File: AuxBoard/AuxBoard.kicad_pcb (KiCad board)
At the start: 2 copper layers, 2 parts, among them J1 ATX-24, J2 RPI4B

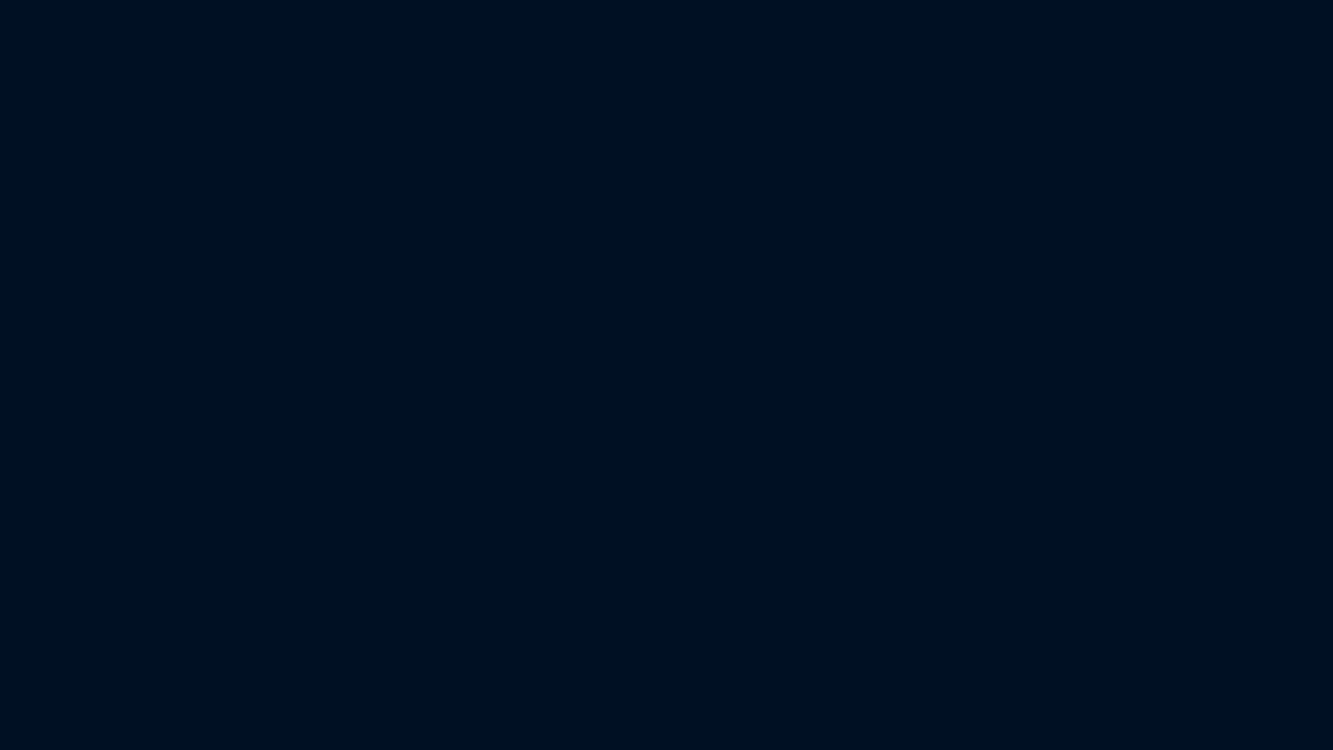
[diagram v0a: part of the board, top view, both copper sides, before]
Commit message: Added headers to handle comms with Matrices and Big LED
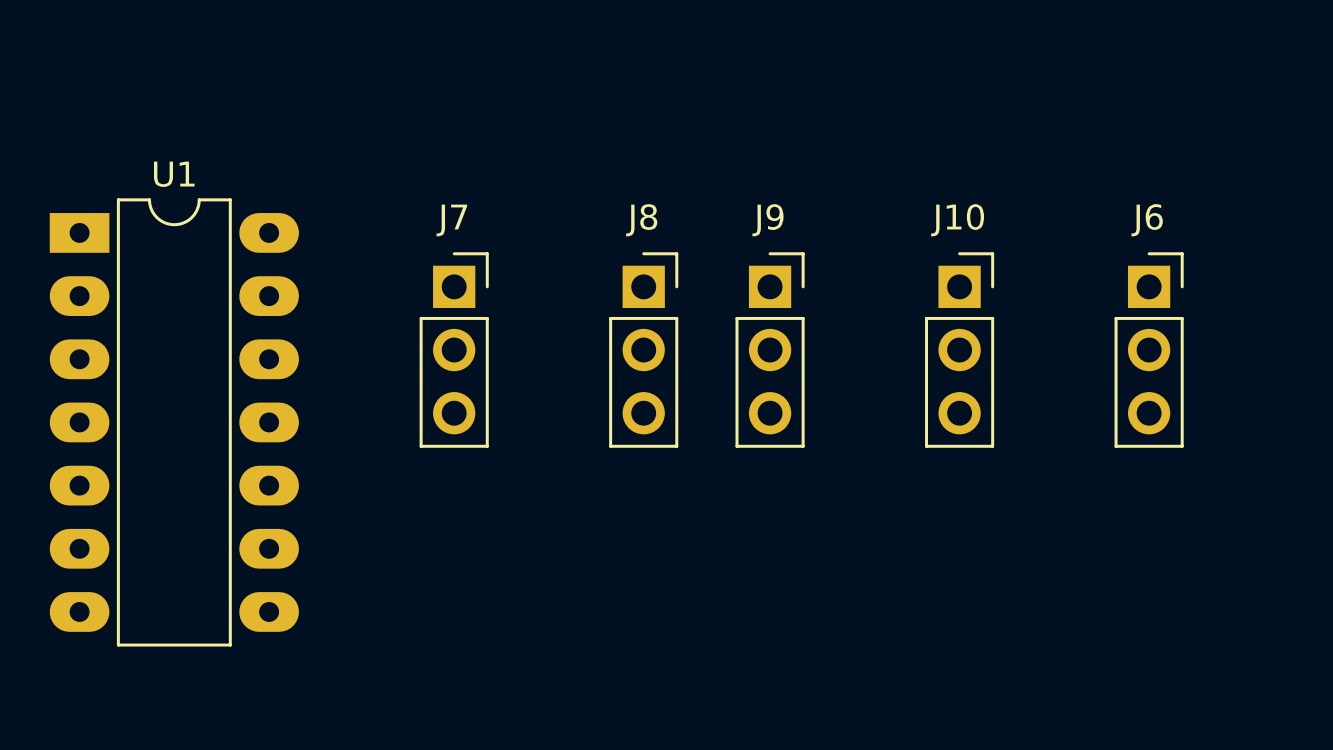
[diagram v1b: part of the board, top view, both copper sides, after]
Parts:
- added J10: MatBIn, Connector_PinSocket_2.54mm:PinSocket_1x03_P2.54mm_Vertical, F.Cu at (68.6, 134.6)
- added J6: BigLED, Connector_PinSocket_2.54mm:PinSocket_1x03_P2.54mm_Vertical, F.Cu at (76.2, 134.6)
- added J7: MatAOut, Connector_PinSocket_2.54mm:PinSocket_1x03_P2.54mm_Vertical, F.Cu at (48.3, 134.6)
- added J8: MatAIn, Connector_PinSocket_2.54mm:PinSocket_1x03_P2.54mm_Vertical, F.Cu at (55.9, 134.6)
- added J9: MatBOut, Connector_PinSocket_2.54mm:PinSocket_1x03_P2.54mm_Vertical, F.Cu at (61.0, 134.6)
- added U1: 74125, Package_DIP:DIP-14_W7.62mm_LongPads, F.Cu at (33.2, 132.5)

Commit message: Power Distro Changes
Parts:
- added J4: MatrixASupply, Connector_PinSocket_2.54mm:PinSocket_1x02_P2.54mm_Vertical, F.Cu at (53.3, 137.2)
- added J5: MatrixBSupply, Connector_PinSocket_2.54mm:PinSocket_1x02_P2.54mm_Vertical, F.Cu at (68.6, 137.2)
- added REF**: MountingHole_2.75mm_RPI_HAT, MountingHole:MountingHole_2.75mm_RPI_HAT, F.Cu at (128.5, 105.4)
- added REF**: MountingHole_2.75mm_RPI_HAT, MountingHole:MountingHole_2.75mm_RPI_HAT, F.Cu at (186.5, 56.1)
- added REF**: MountingHole_2.75mm_RPI_HAT, MountingHole:MountingHole_2.75mm_RPI_HAT, F.Cu at (186.5, 79.4)
- added REF**: MountingHole_2.75mm_RPI_HAT, MountingHole:MountingHole_2.75mm_RPI_HAT, F.Cu at (128.5, 79.4)
- added REF**: MountingHole_2.75mm_RPI_HAT, MountingHole:MountingHole_2.75mm_RPI_HAT, F.Cu at (128.5, 56.1)
- added REF**: MountingHole_2.75mm_RPI_HAT, MountingHole:MountingHole_2.75mm_RPI_HAT, F.Cu at (186.5, 105.4)
- J2: footprint Connector_PinSocket_2.54mm:PinSocket_2x19_P2.54mm_Vertical_SMD -> Connector_PinSocket_2.54mm:PinSocket_2x20_P2.54mm_Vertical_SMD; moved to B.Cu
- moved J2 97.0 mm to (157.5, 56.0), turned to -90 degrees
- moved J10 5.08 mm to (73.7, 134.6)
- moved J6 5.08 mm to (81.3, 134.6)
- moved J8 2.54 mm to (58.4, 134.6)
- moved J9 2.54 mm to (63.5, 134.6)
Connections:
- J1 pad 1: unconnected-(J1-Pad1) -> +3.3V
- J1 pad 12: unconnected-(J1-Pad1) -> +3.3V
- J1 pad 13: unconnected-(J1-Pad1) -> +3.3V
- J1 pad 15: +5VP -> GND
- J1 pad 17: +5VP -> GND
- J1 pad 18: +5VP -> GND
- J1 pad 19: +5VP -> GND
- J1 pad 2: unconnected-(J1-Pad1) -> +3.3V
- J1 pad 24: +5VP -> GND
- J1 pad 3: +5VP -> GND
- J1 pad 5: +5VP -> GND
- J1 pad 7: +5VP -> GND
- J10 pad 1: +5VP -> GND
- J2 pad 14: +5VP -> GND
- J2 pad 20: +5VP -> GND
- J2 pad 25: +5VP -> GND
- J2 pad 30: +5VP -> GND
- J2 pad 34: +5VP -> GND
- J2 pad 4: 5V_Power -> Net-(F5-Pad1)
- J2 pad 6: +5VP -> GND
- J2 pad 9: +5VP -> GND
- J6 pad 1: +5VP -> GND
- J7 pad 1: +5VP -> GND
- J8 pad 1: +5VP -> GND
- J9 pad 1: +5VP -> GND
- U1 pad 1: +5VP -> GND
- U1 pad 7: +5VP -> GND

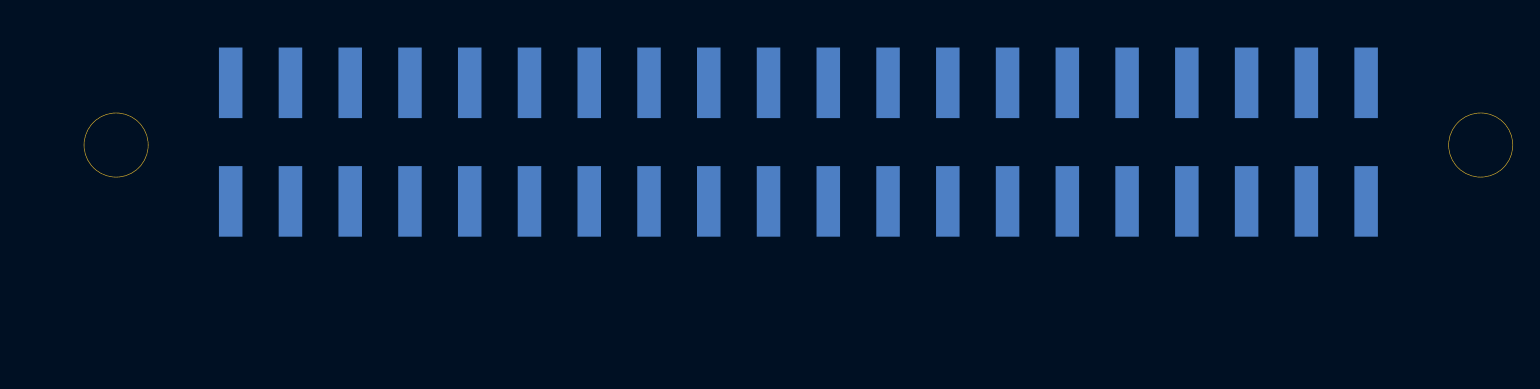
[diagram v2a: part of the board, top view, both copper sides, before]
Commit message: Added seccond GPIO
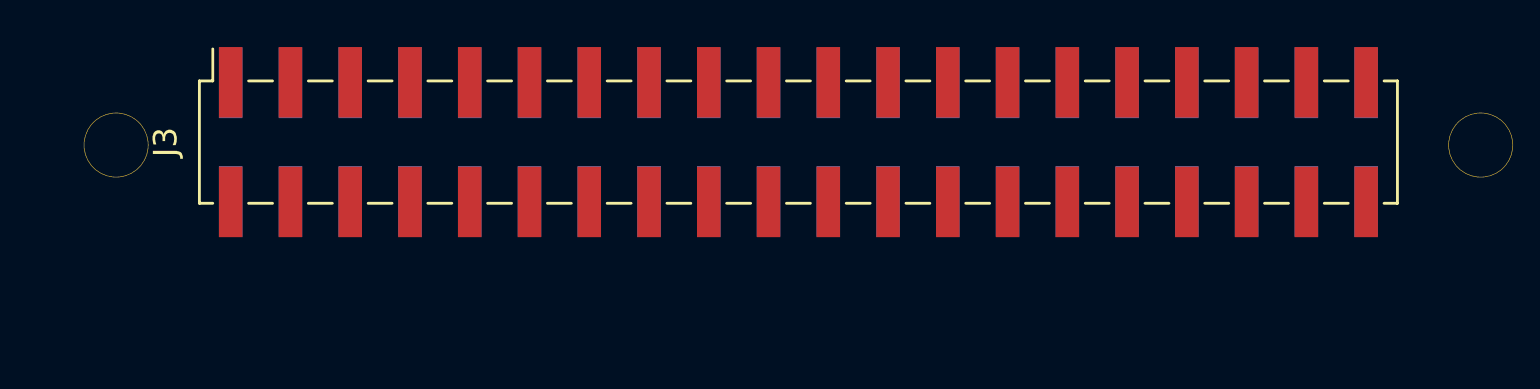
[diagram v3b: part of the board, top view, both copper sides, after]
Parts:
- added J3: Passthrough, Connector_PinSocket_2.54mm:PinSocket_2x20_P2.54mm_FLIPED_Vertical_SMD, F.Cu at (157.5, 56.0)
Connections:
- net Net-(F5-Pad1) renamed /5V_Power
- net Net-(J2-Pad19) renamed /MOSI
- J2 pad 1: unconnected-(J2-Pad1) -> /3V3_Power
- J2 pad 10: unconnected-(J2-Pad10) -> /GPIO_15
- J2 pad 11: unconnected-(J2-Pad11) -> /GPIO_17
- J2 pad 12: unconnected-(J2-Pad12) -> /GPIO_18
- J2 pad 13: unconnected-(J2-Pad13) -> /GPIO_27
- J2 pad 15: unconnected-(J2-Pad15) -> /GPIO_22
- J2 pad 16: unconnected-(J2-Pad16) -> /GPIO_23
- J2 pad 17: unconnected-(J2-Pad17) -> /3V3_Power
- J2 pad 18: unconnected-(J2-Pad18) -> /GPIO_24
- J2 pad 22: unconnected-(J2-Pad22) -> /GPIO_25
- J2 pad 24: unconnected-(J2-Pad24) -> /GPIO_8
- J2 pad 26: unconnected-(J2-Pad26) -> /GPIO_7
- J2 pad 27: unconnected-(J2-Pad27) -> /GPIO_0
- J2 pad 28: unconnected-(J2-Pad28) -> /GPIO_1
- J2 pad 29: unconnected-(J2-Pad29) -> /GPIO_5
- J2 pad 3: unconnected-(J2-Pad3) -> /GPIO_2
- J2 pad 31: unconnected-(J2-Pad31) -> /GPIO_6
- J2 pad 32: unconnected-(J2-Pad32) -> /GPIO_12
- J2 pad 33: unconnected-(J2-Pad33) -> /GPIO_13
- J2 pad 35: unconnected-(J2-Pad35) -> /GPIO_19
- J2 pad 36: unconnected-(J2-Pad36) -> /GPIO_16
- J2 pad 37: unconnected-(J2-Pad37) -> /GPIO_26
- J2 pad 38: unconnected-(J2-Pad38) -> /GPIO_20
- J2 pad 40: unconnected-(J2-Pad40) -> /GPIO_21
- J2 pad 5: unconnected-(J2-Pad5) -> /GPIO_3
- J2 pad 7: unconnected-(J2-Pad7) -> /GPIO_4
- J2 pad 8: unconnected-(J2-Pad8) -> /GPIO_14

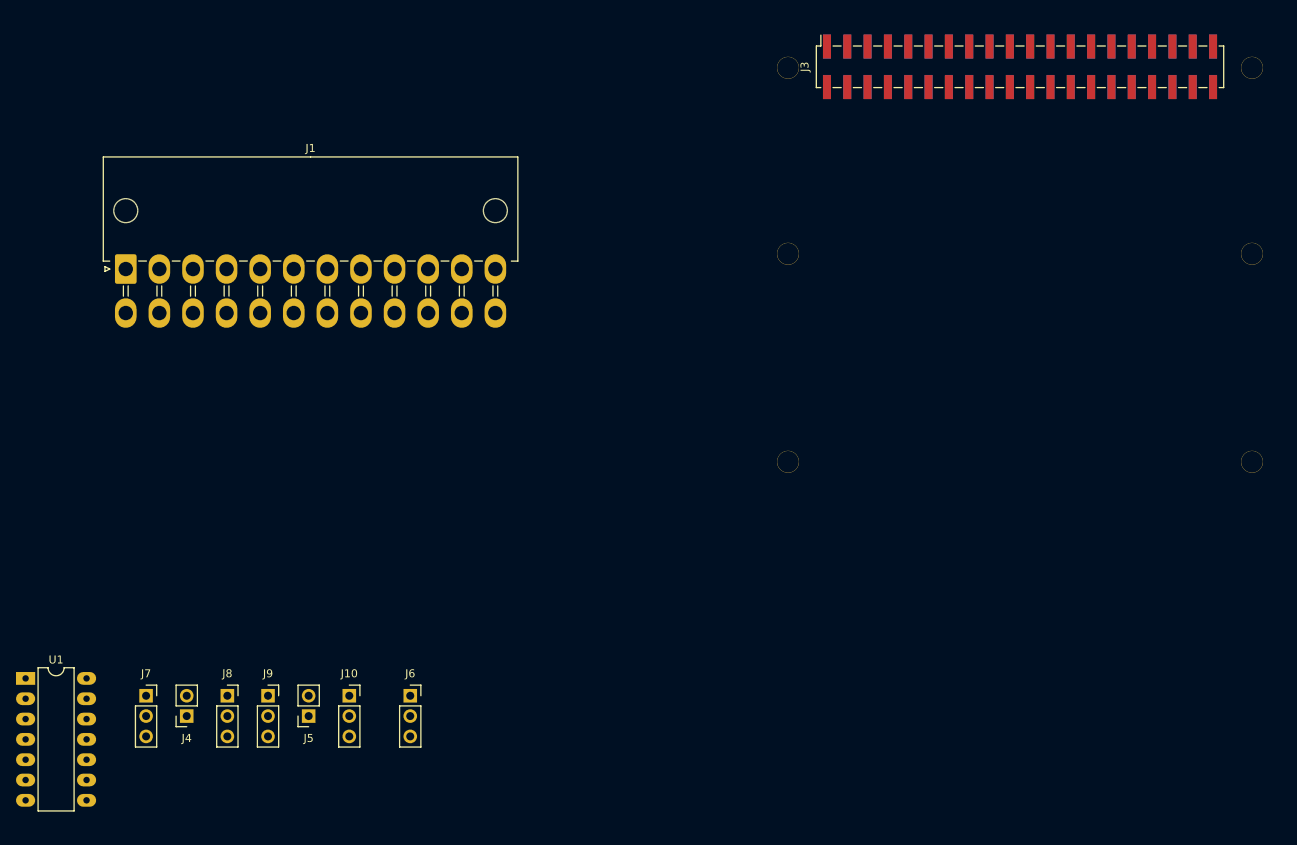
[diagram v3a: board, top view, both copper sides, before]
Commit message: Draft Schematic Finished. Added ZVD and Changed to polyfuses
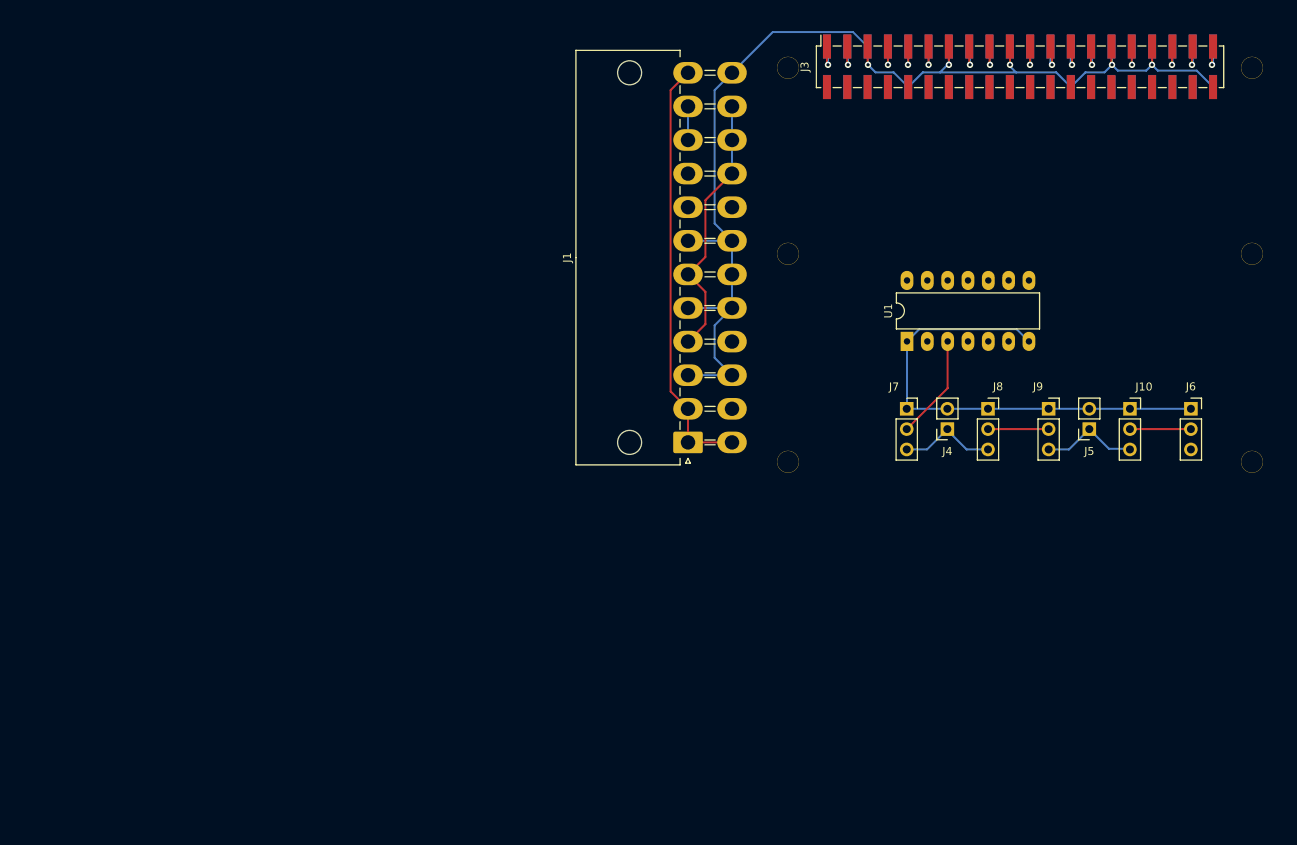
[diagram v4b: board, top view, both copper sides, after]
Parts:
- moved U1 118.0 mm to (143.4, 90.3), turned to 90 degrees
- moved J10 104.0 mm to (171.2, 98.8)
- moved J6 104.0 mm to (178.9, 98.8)
- moved J9 104.0 mm to (161.1, 98.8)
- moved J5 104.0 mm to (166.2, 101.3)
- moved J7 101.6 mm to (143.3, 98.8)
- moved J8 101.6 mm to (153.5, 98.8)
- moved J4 101.6 mm to (148.4, 101.3)
- moved J1 73.5 mm to (116.0, 103.0), turned to 90 degrees
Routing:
- net GND: track 0.00 -> 212.5 mm, vias 0 -> 5
- net +3.3V: track 0.00 -> 53.5 mm
- net +5V: track 0.00 -> 33.5 mm
- net DOUT: track 0.00 -> 13.1 mm
- net 5VMatA: track 0.00 -> 12.3 mm
- net 5VMatB: track 0.00 -> 12.3 mm
- net /5V_Power: track 0.00 -> 9.30 mm, vias 0 -> 2
- net DOUTMatB: track 0.00 -> 7.62 mm
- net DOUTMatA: track 0.00 -> 7.58 mm
- net /GPIO_8: track 0.00 -> 4.72 mm, vias 0 -> 1
- net /GPIO_7: track 0.00 -> 4.68 mm, vias 0 -> 1
- net /GPIO_21: track 0.00 -> 4.67 mm, vias 0 -> 1
- net /GPIO_1: track 0.00 -> 4.65 mm, vias 0 -> 1
- net /GPIO_23: track 0.00 -> 4.64 mm, vias 0 -> 1
- net /GPIO_20: track 0.00 -> 4.63 mm, vias 0 -> 1
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
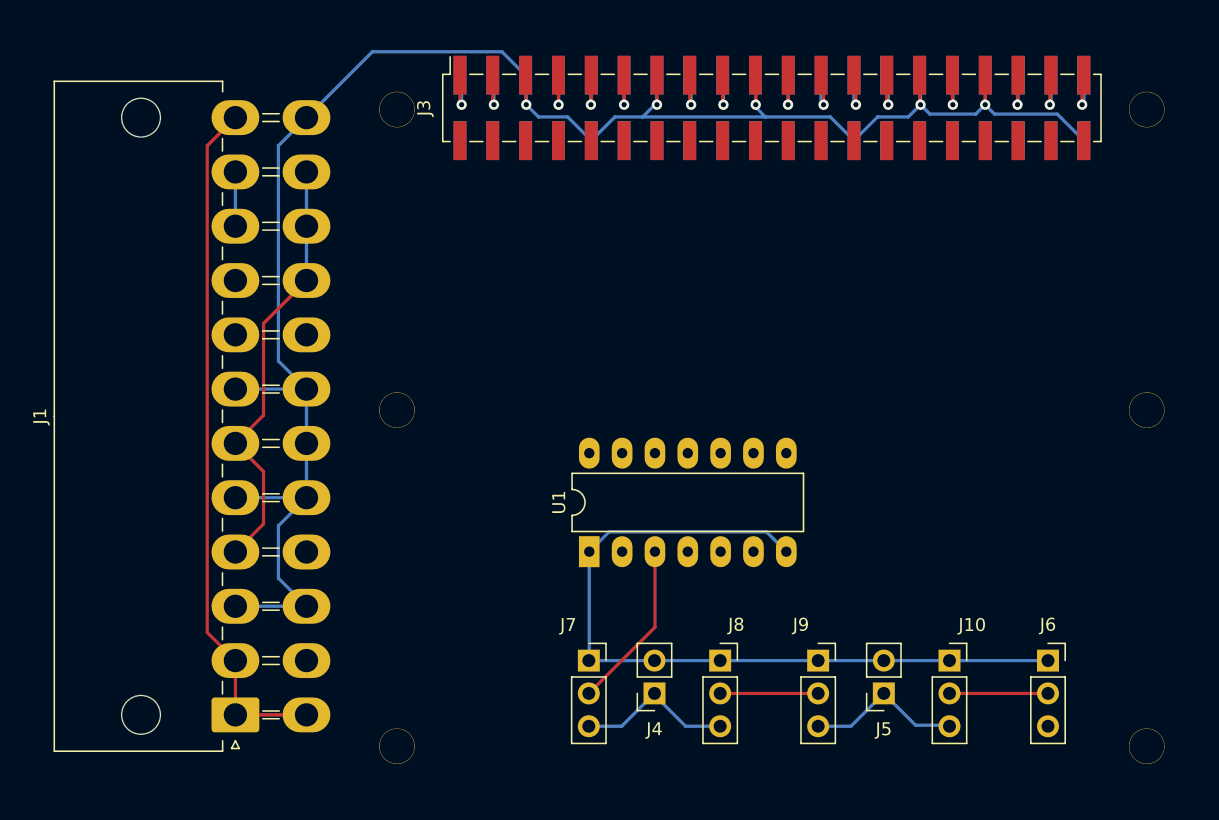
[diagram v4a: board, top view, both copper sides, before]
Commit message: Added fan header and mosfet control for PI power supply
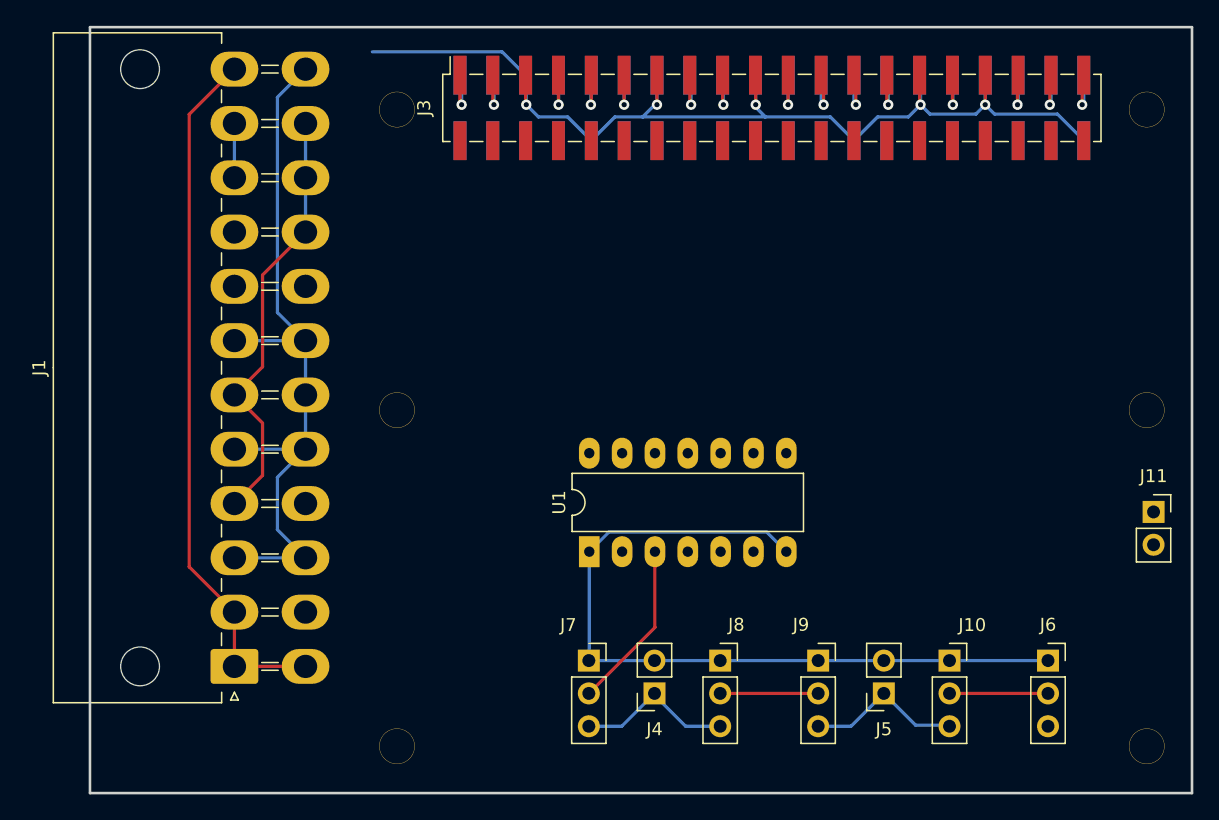
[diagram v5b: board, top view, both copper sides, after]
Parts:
- added J11: FanHeader, Connector_PinSocket_2.54mm:PinSocket_1x02_P2.54mm_Vertical, F.Cu at (187.0, 87.2)
- moved J1 3.75 mm to (115.9, 99.2)
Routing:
- net GND: track 212.5 -> 205.3 mm
- net +3.3V: track 53.5 -> 54.6 mm
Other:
- board outline added: 85.2 x 59.2 mm
